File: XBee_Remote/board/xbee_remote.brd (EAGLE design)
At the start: 96.5 x 64.8 mm, 39 parts, among them IC1 AVR-MEGA8-PPTH, IC2 74LS125N, IC5 74LS595N, J1 1X2-3.5MM, J2 AVR_SPI_PRG, Y1 RESONATORPTH

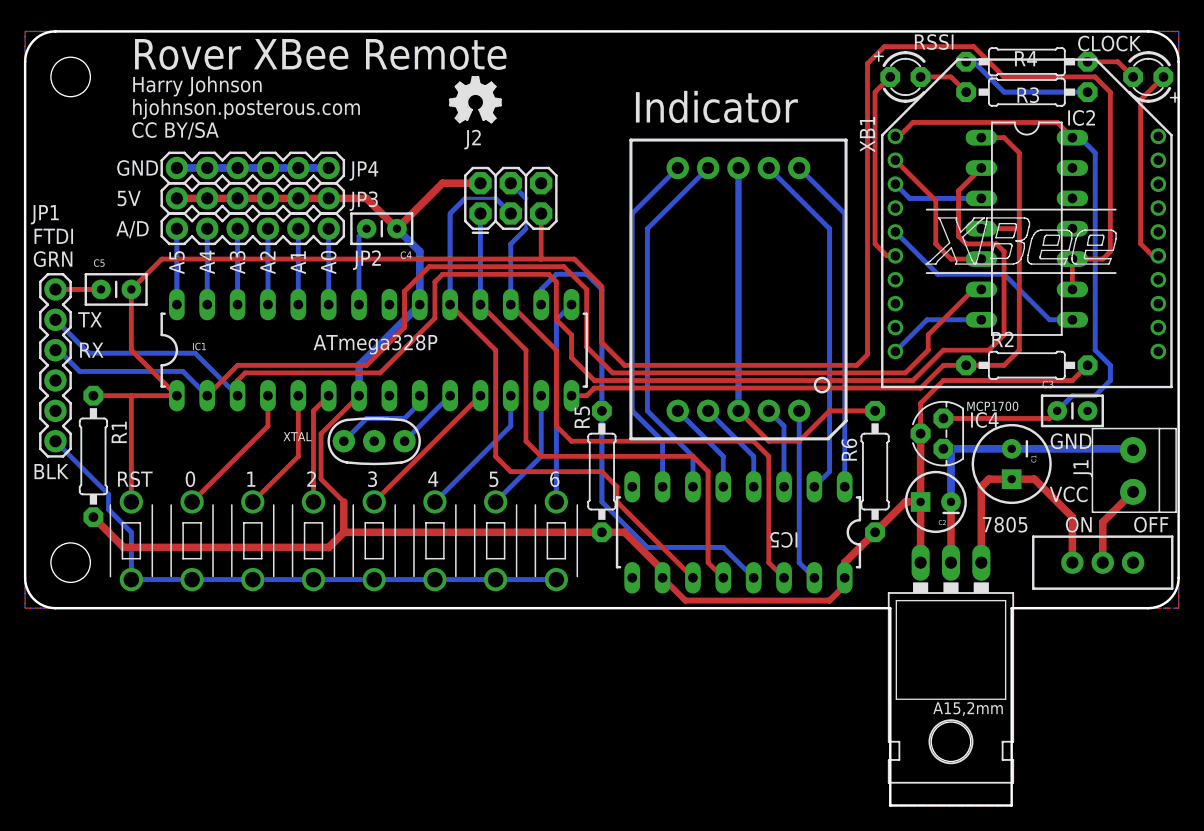
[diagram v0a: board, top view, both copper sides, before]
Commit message: Updated through-hole board and schematic
Changed polygon fill to hatch, fully routed the board to not need
polygon, just in case, cleaned up the schematic, and added a net list
to the schematic.
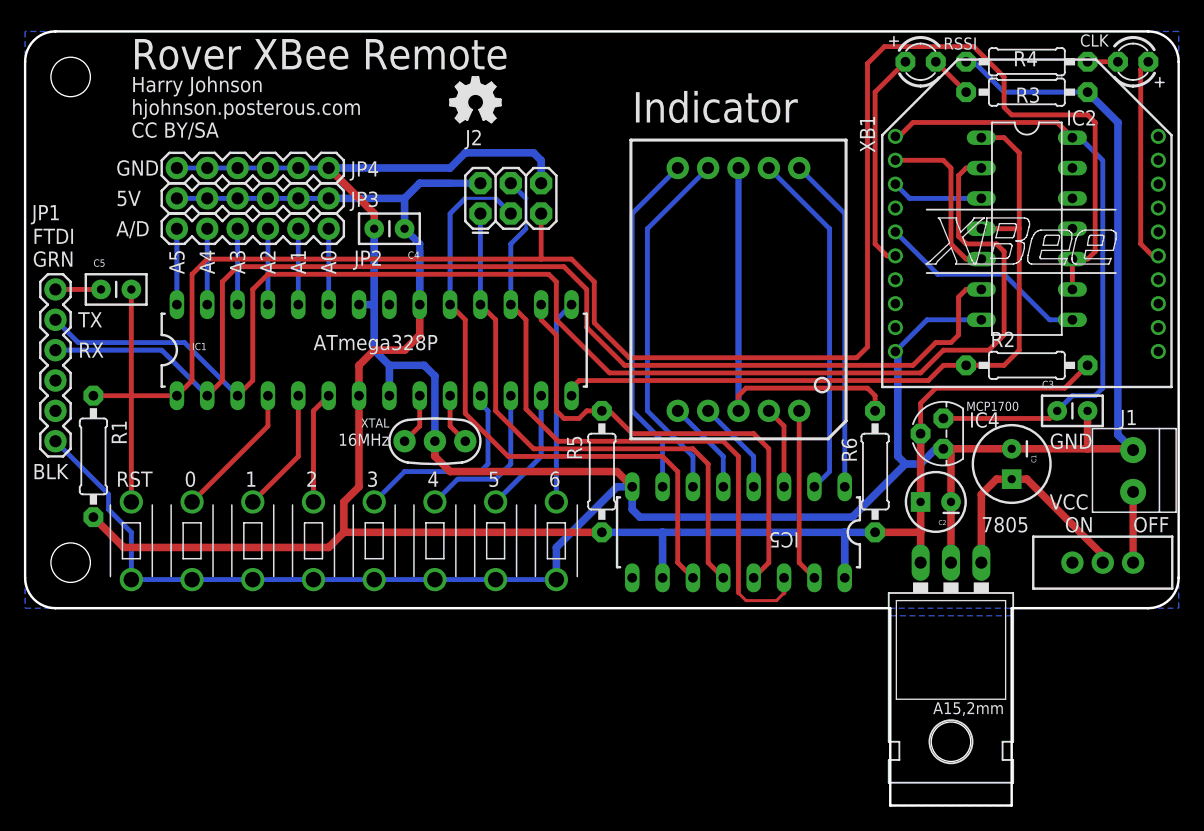
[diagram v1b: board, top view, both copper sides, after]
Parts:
- removed CLOCK: (no value), adafruit:LED3MM
- added CLK: (no value), adafruit:LED3MM
- moved Y1 5.08 mm to (34.3, 30.5)
- moved RSSI 1.80 mm to (74.9, 62.2)
- moved C4 0.64 mm to (31.8, 48.3)
- turned S1 to 270 degrees
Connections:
- net N$18 renamed A0
- net N$19 renamed A1
- net N$20 renamed A2
- net N$21 renamed A3
- net N$22 renamed SDA
- net N$23 renamed SCL
- removed net N$6: J1.2, S1.2
- new net N$4: J1.2, S1.1
- net N$26: now also CLK.A; no longer CLOCK.A
- net N$27: now also CLK.K; no longer CLOCK.K
- net N$5: now also S1.2; no longer S1.1
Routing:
- net GND: track 115.1 -> 265.1 mm
- net N$6: track 6.97 -> 0.00 mm
- net N$4: track 0.00 -> 5.92 mm
- net DS: track 52.5 -> 56.9 mm
- net IO3: track 12.6 -> 16.8 mm
- net N$1: track 8.30 -> 4.34 mm
- net SH_CP: track 49.5 -> 52.6 mm
- net RX: track 95.4 -> 98.1 mm
- net IO4: track 11.5 -> 13.4 mm
- net N$24: track 16.6 -> 18.4 mm
- net N$27: track 4.34 -> 2.54 mm
- net 3V3_RX: track 12.7 -> 14.3 mm
- net N$2: track 5.39 -> 4.34 mm
- net TX: track 114.8 -> 115.8 mm
- net N$10: track 33.9 -> 34.8 mm
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- added copper zone on layer 16, net N$3
- removed copper zone on layer 1, net GND
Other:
- board text added: "16MHz"
- board text removed: "UI/Microprocessor block"

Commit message: Made a bunch of changes.
Most importantly: Switched the lines for Switch 6 and XBee enable, to
make routing more sensible, and to make reading of switches take a
single for loop.
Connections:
- net /XBEE_ENABLE: now also IC1.15; no longer IC1.14
- net IO6: now also IC1.14; no longer IC1.15
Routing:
- net IO6: track 17.0 -> 9.42 mm
- net TX: track 115.8 -> 120.3 mm
- net /XBEE_ENABLE: track 64.1 -> 67.9 mm
- net RX: track 98.1 -> 101.1 mm
- net LATCHENABLE: track 40.4 -> 37.6 mm
- net GND: track 265.1 -> 263.5 mm
- net /RES: track 165.1 -> 166.6 mm
- net 5V: track 165.5 -> 166.8 mm
- net DS: track 56.9 -> 56.3 mm
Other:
- board text added: "github.com/hjohnson"
- board text removed: "hjohnson.posterous.com"
